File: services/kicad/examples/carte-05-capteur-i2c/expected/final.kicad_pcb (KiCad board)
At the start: 2 copper layers, 43.5 x 32.5 mm, 26 parts, among them J1 IN_5V, J2 SWD, J3 I2C, U1 STM32F103C8T6, U2 AMS1117-3.3, U3 BME280

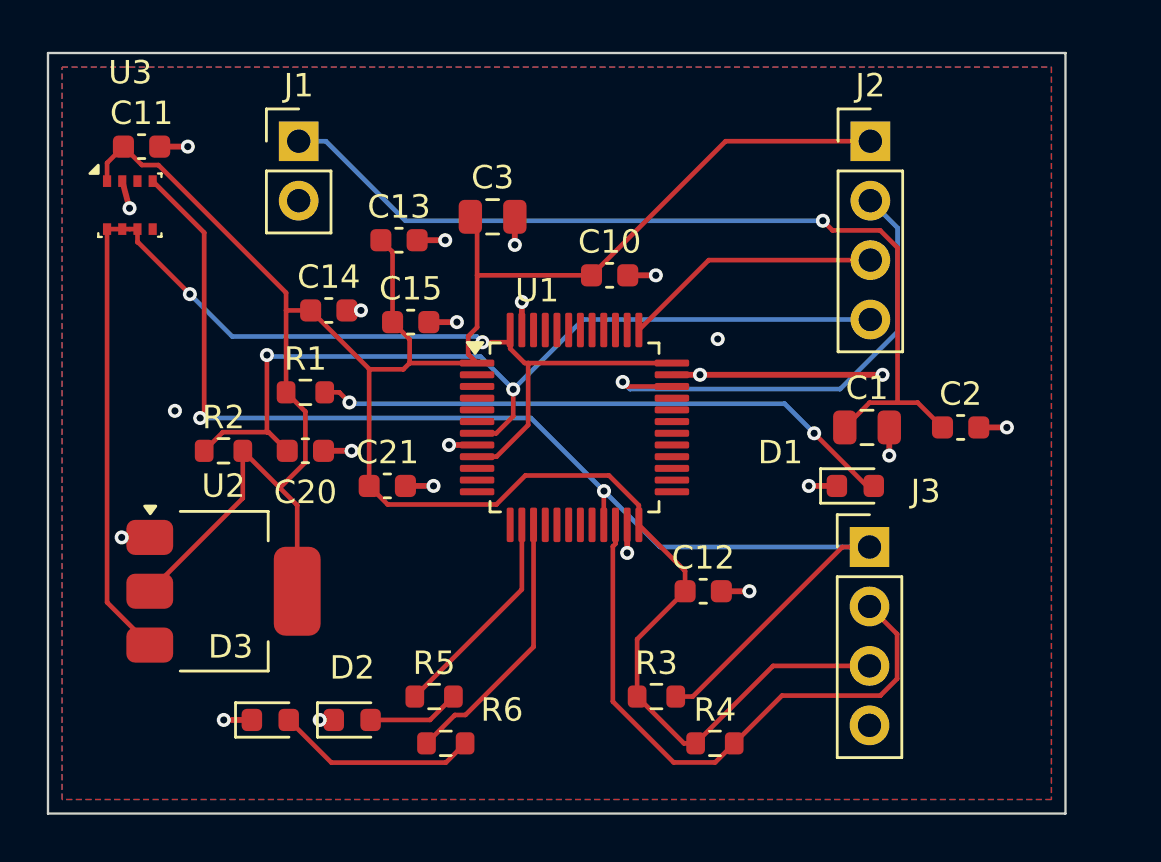
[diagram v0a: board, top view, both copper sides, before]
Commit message: feat(placement): les peripheriques se REPARTISSENT, ils ne s empilent plus
Question de l utilisateur devant le rendu : « c est quoi ce type de placement ? ».
Les composants s entassaient d un seul cote du boitier, etiquettes de
serigraphie l une sur l autre, trois quarts de la couronne vides.

TROIS CAUSES, toutes dans `_poser_les_peripheriques`, toutes la meme faute —
un angle unique pour tout un groupe :

  - les DIRECTS qui visent la meme broche (tous les decouplages d un rail,
    toutes les resistances d un meme signal) recevaient le MEME `angle_vers`
    et le meme rayon de depart ;
  - les SUIVEURS d un meme parent recevaient tous atan2(parent - centre) ;
  - les ISOLES partaient tous de l angle 0.0, c est-a-dire du meme point.

`le_long_du_rayon` ne s ecartait qu une fois la place prise : d ou la file.

REMEDE : `_ecart_en_eventail`. Le PREMIER de chaque groupe garde EXACTEMENT la
direction calculee — c est la topologie, on ne la perd pas pour faire joli — et
les suivants s ecartent symetriquement de 3 x `_PAS_ANGLE_DEG`.
Rien de deja pose ne bouge : seul l ANGLE DE DEPART de la recherche change, et
`le_long_du_rayon` reste seul juge de ce qui est libre.

BANC DES DIX CARTES, contour resserre ET peripheriques repartis :

    carte             demandee    livree         err  manq
    carte-01           25 x 20    20,1 x 13,6     0    0
    carte-02           55 x 40    34,9 x 25,2     0    0
    carte-03           50 x 35    27,6 x 19,9     0    0
    carte-04           60 x 45    36,6 x 29,8     0    0
    carte-05           70 x 50    40,0 x 32,6     0    0
    carte-06           80 x 60    46,5 x 36,4     0    0
    carte-07          110 x 80    47,7 x 38,8     0    0
    carte-08          125 x 95    57,4 x 44,1     0    0
    carte-09          130 x 100   57,8 x 45,2     0    0
    carte-10          140 x 105   59,0 x 45,8     0    0

Dix sur dix, 100 % route. carte-07 gagne 5,5 mm de largeur sur le passage
precedent, carte-06 deux, carte-10 deux. Sur ca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
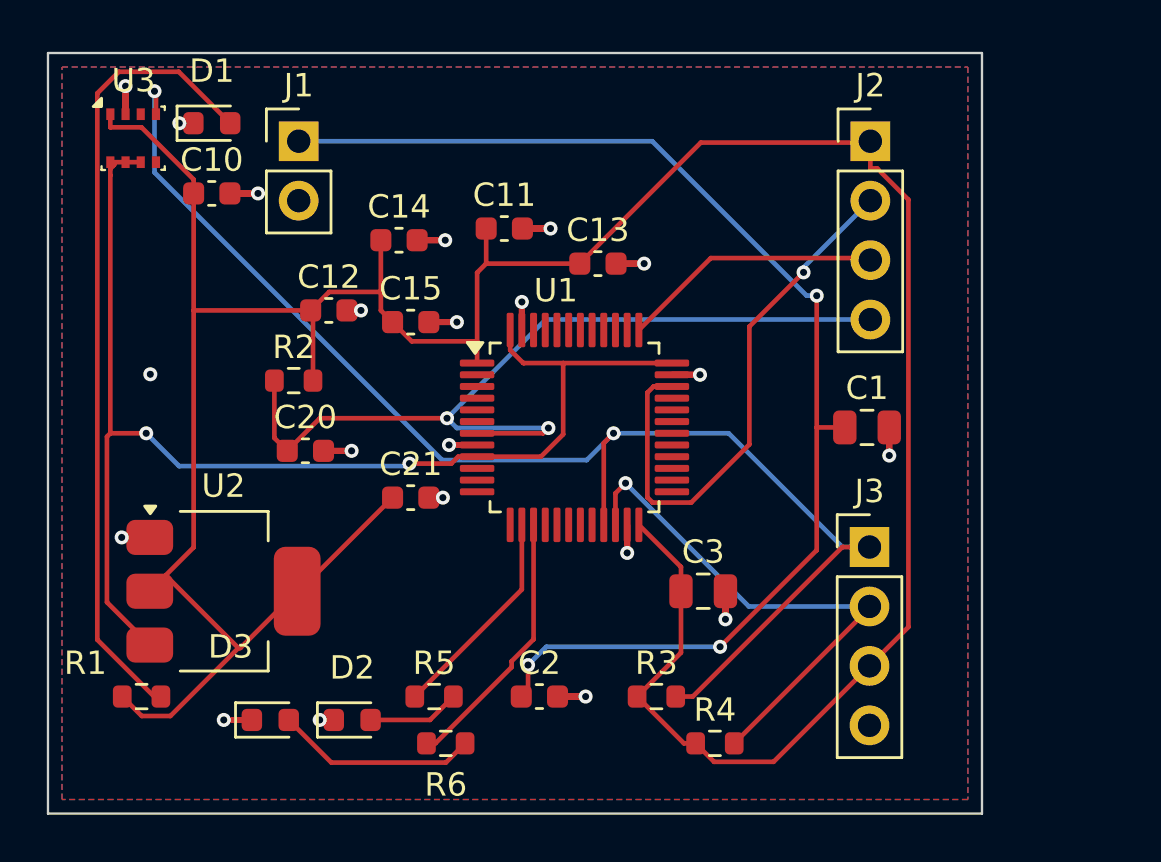
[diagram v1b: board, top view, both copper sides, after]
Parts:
- moved D1 31.6 mm to (120.5, 83.0)
- moved C2 21.4 mm to (134.5, 107.5)
- moved C12 20.0 mm to (125.5, 91.0)
- moved C3 18.4 mm to (141.5, 103.0)
- moved C10 17.4 mm to (120.5, 86.0)
- moved C11 15.9 mm to (133.0, 87.5)
- moved R1 14.8 mm to (117.5, 107.5)
- moved C13 8.56 mm to (137.0, 89.0)
- moved C14 4.24 mm to (128.5, 88.0)
- moved R2 4.24 mm to (124.0, 94.0)
- moved U3 2.86 mm to (117.1, 83.6)
- moved C21 1.12 mm to (129.0, 99.0)
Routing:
- net GND: track 30.6 -> 69.6 mm, vias 23 -> 21
- net +3V3: track 115.8 -> 132.7 mm
- net VIN: track 39.1 -> 52.8 mm, vias 1 -> 3
- net LED_PWR: track 25.1 -> 34.0 mm, vias 2 -> 0
- net SCL: track 54.4 -> 57.6 mm
- net SDA: track 25.9 -> 22.8 mm, vias 0 -> 1
- net PWR_FLAG: track 51.4 -> 54.5 mm
- net SWDIO: track 21.2 -> 23.7 mm
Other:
- board size 43.5 x 32.5 mm -> 39.9 x 32.5 mm

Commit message: docs(banc): les dix boards du banc du 2026-09-23, service corrige
Artefacts du banc dont le tableau est deja commite : les dix cartes a
100 % route, 0 erreur, 0 connexion manquante, chacune a la taille de son
circuit.

Co-Authored-By: Claude Opus 5 <noreply@anthropic.com>
Claude-Session: https://claude.ai/code/session_01TnMqm4La2CxQHHB5K8aSSV
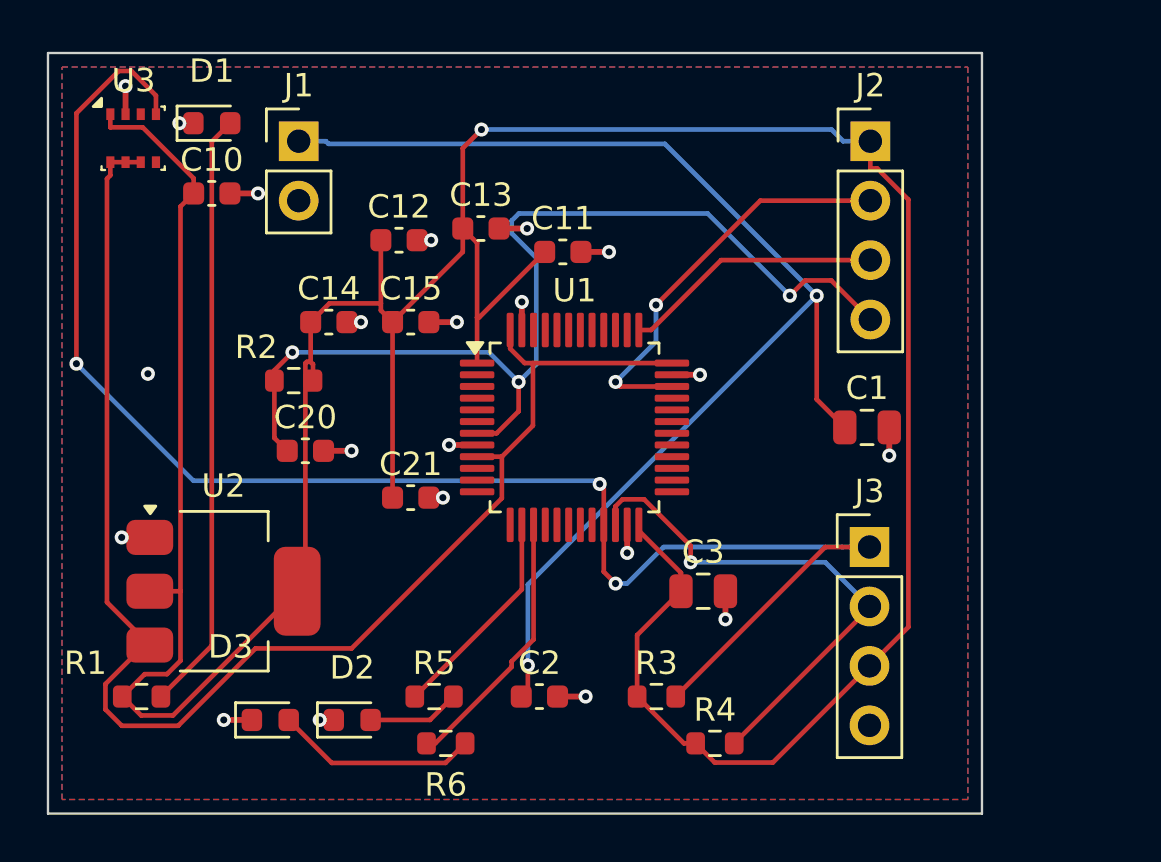
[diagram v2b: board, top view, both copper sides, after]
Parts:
- moved C13 5.22 mm to (132.0, 87.5)
- moved C14 4.61 mm to (125.5, 91.5)
- moved C12 4.24 mm to (128.5, 88.0)
- moved C11 2.69 mm to (135.5, 88.5)
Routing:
- net GND: track 69.6 -> 21.0 mm
- net +3V3: track 132.7 -> 149.8 mm, vias 0 -> 1
- net SCL: track 57.6 -> 67.5 mm, vias 2 -> 3
- net PWR_FLAG: track 54.5 -> 63.0 mm, vias 2 -> 0
- net LED_PWR: track 34.0 -> 25.7 mm
- net SWDIO: track 23.7 -> 17.5 mm, vias 1 -> 2
- net NRST: track 38.1 -> 43.9 mm, vias 2 -> 3
- net VIN: track 52.8 -> 53.4 mm, vias 3 -> 2

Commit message: fix(banc): le banc route comme la production — plafond 8, budget du client
D-2026-09-24-f. run_pipeline.py prenait 2 couches et 1800 s par défaut, et
carte-07 écrivait 2 en dur : dix cartes sur quinze ne pouvaient jamais
escalader, et la règle « toute connexion manquante fait monter » était
inerte dans le banc. Mesuré sur carte-07 : 97 %, seule la masse manquante,
« le palier suivant sera tenté »… puis retour à 2 couches.

Plafond par défaut 8 (client Pro Max), budget min(600 + 300 x plafond, 3600)
comme routingSearchBudgetS côté client. En production, rien ne change : le
plafond reste celui du plan.

Livraisons du jour, toutes vérifiées par kicad-cli et contre le schéma
(0 erreur bloquante, 0 connexion manquante, 0 court-circuit) :
carte-04, 05, 06, 08 (campagne de l'après-midi) et carte-09, 10 (4 couches).
Les boards versionnés de ces cartes court-circuitaient des nets du schéma.

Correction de ma propre erreur dans la doc : carte-07 n'avait jamais
escaladé ; les lignes « palier 4 et 6 » du journal étaient celles de
carte-08, démarrée la même minute.

Co-Authored-By: Claude Opus 5.5 <noreply@anthropic.com>
Claude-Session: https://claude.ai/code/session_01TnMqm4La2CxQHHB5K8aSSV
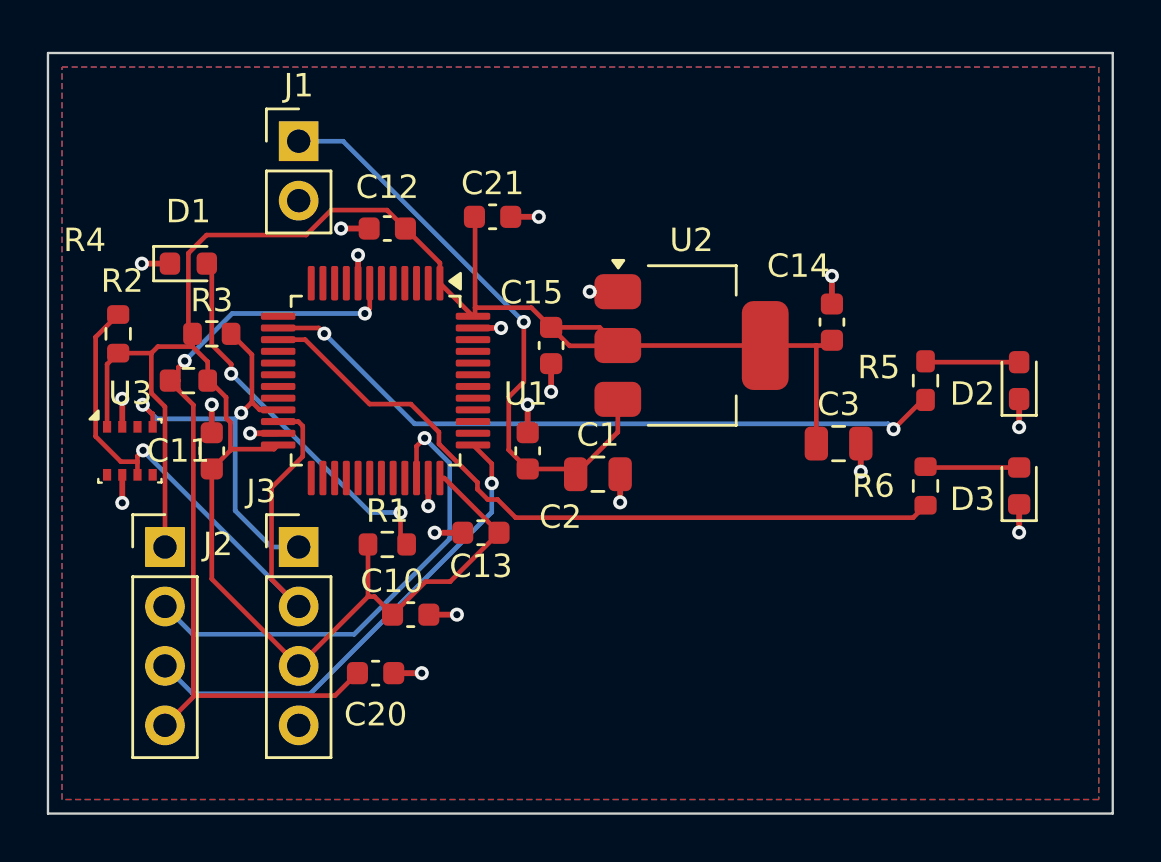
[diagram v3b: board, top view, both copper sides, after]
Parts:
- moved J2 34.8 mm to (118.5, 101.1)
- moved D3 33.5 mm to (155.0, 98.5), turned to 90 degrees
- moved D2 32.0 mm to (155.0, 94.0), turned to 90 degrees
- moved R4 30.9 mm to (116.5, 92.0), turned to 90 degrees
- moved R5 25.0 mm to (151.0, 94.0), turned to 90 degrees
- moved R3 24.5 mm to (120.5, 92.0)
- moved J3 24.4 mm to (124.2, 101.1)
- moved R6 23.3 mm to (151.0, 98.5), turned to 90 degrees
- moved U2 22.6 mm to (141.0, 92.5)
- moved C14 21.5 mm to (147.0, 91.5), turned to 90 degrees
- moved C10 19.9 mm to (129.0, 104.0)
- moved C11 17.2 mm to (120.5, 97.0), turned to 90 degrees
- moved U3 13.4 mm to (117.0, 97.0)
- moved C13 13.0 mm to (132.0, 100.5), turned to 180 degrees
- moved C21 12.5 mm to (132.5, 87.0)
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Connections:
- U1 pad 36: PWR_FLAG -> +3V3
- U1 pad 48: PWR_FLAG -> +3V3
- U1 pad 9: PWR_FLAG -> Net-(U1-9)
- U2 pad 3: PWR_FLAG -> VIN
- U3 pad 6: PWR_FLAG -> SDA
- U3 pad 7: PWR_FLAG -> GND
- U3 pad 8: PWR_FLAG -> Net-(U3-8)
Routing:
- net PWR_FLAG: track 63.0 -> 0.00 mm
- net +3V3: track 149.8 -> 97.8 mm, vias 1 -> 0
- net SCL: track 67.5 -> 18.2 mm, vias 3 -> 2
- net VIN: track 53.4 -> 25.8 mm, vias 2 -> 1
- net IO_ST1: track 9.23 -> 30.0 mm, vias 0 -> 2
- net IO_ST2: track 11.5 -> 31.5 mm
- net SWCLK: track 11.1 -> 20.9 mm, vias 0 -> 1
- net NRST: track 43.9 -> 34.2 mm, vias 3 -> 2
- net LED_PWR: track 25.7 -> 16.3 mm, vias 0 -> 2
- net SDA: track 22.3 -> 28.3 mm
- net LED2_A: track 8.65 -> 4.02 mm
- net GND: track 21.0 -> 25.2 mm
- net SWDIO: track 17.5 -> 20.9 mm, vias 2 -> 1
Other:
- board size 39.9 x 32.5 mm -> 45.5 x 32.5 mm
